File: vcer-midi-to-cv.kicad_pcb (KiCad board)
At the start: 4 copper layers, 140 x 128.5 mm, 109 parts, among them J1 Conn_01x10_Male, J10 CV3, J11 CV4, J12 Vel1, J13 Vel2, J14 Vel3, J15 Vel4, J16 Gate1, J17 Gate2, J18 Gate3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

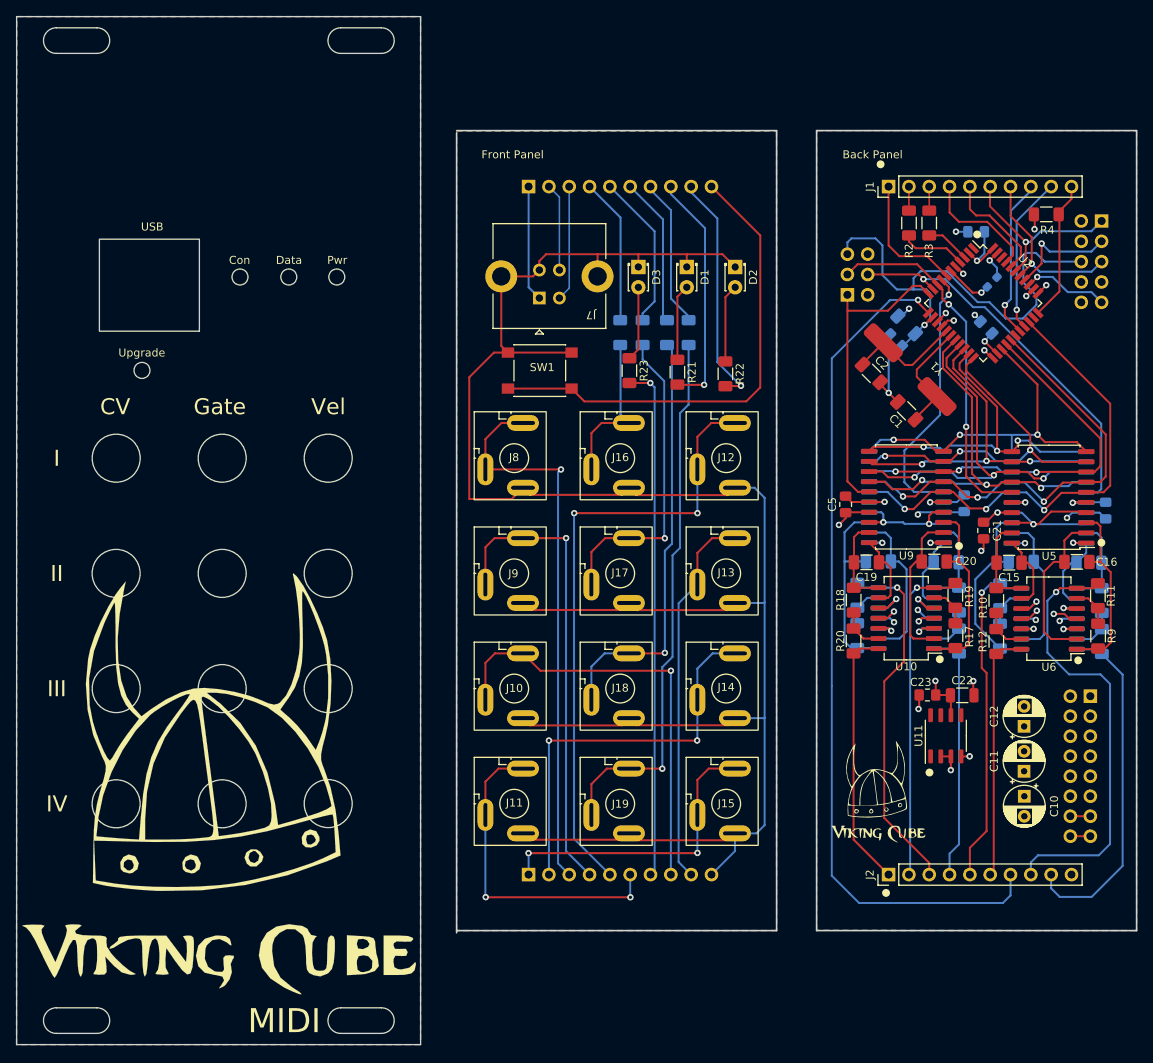
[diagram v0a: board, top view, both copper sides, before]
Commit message: removed other panels
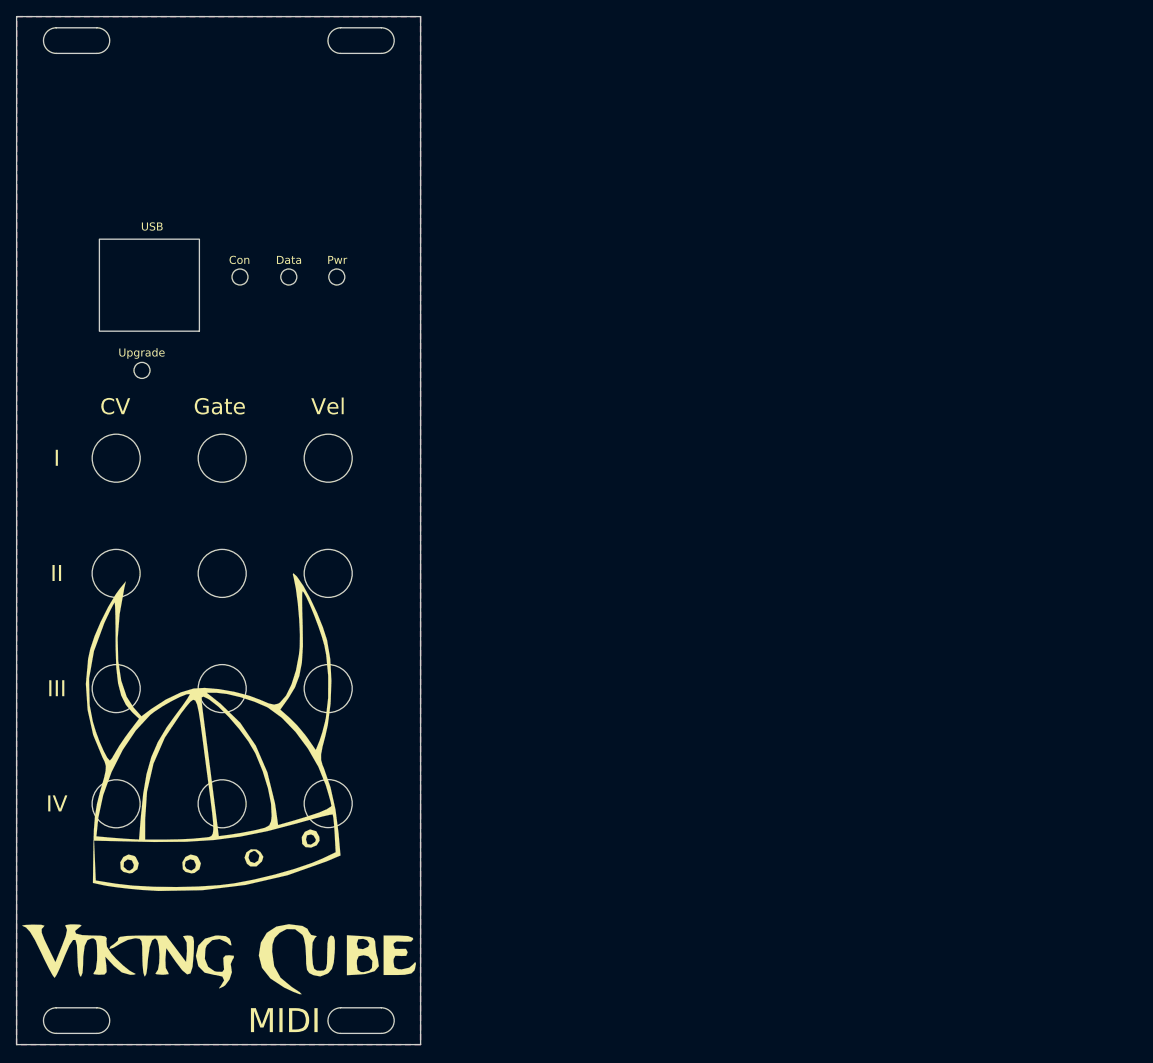
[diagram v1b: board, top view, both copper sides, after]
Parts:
- removed C1, C2: 18pF, Capacitor_SMD:C_1206_3216Metric_Pad1.33x1.80mm_HandSolder
- removed C10, C11, C12: 100uF, Capacitor_THT:CP_Radial_D5.0mm_P2.50mm
- removed C13, C14, C15, C16, C17, C18, C19, C20: 15pF, Capacitor_SMD:C_1206_3216Metric_Pad1.33x1.80mm_HandSolder
- removed C21, C3, C5, C6, C7, C8, C9: 100nF, Capacitor_SMD:C_0805_2012Metric_Pad1.18x1.45mm_HandSolder
- removed C22: 1uF (TANT), Capacitor_SMD:C_1206_3216Metric
- removed C23: 100nF (Ceramic), Capacitor_SMD:C_0805_2012Metric_Pad1.18x1.45mm_HandSolder
- removed C4: 1u, Capacitor_SMD:C_0603_1608Metric_Pad1.08x0.95mm_HandSolder
- removed D1, D2, D3: LED, LED_THT:LED_D1.8mm_W3.3mm_H2.4mm
- removed the G*** at (55.0, 84.6)
- removed the G*** at (6.69, 30.3)
- removed J1, J2: Conn_01x10_Male, Connector_PinHeader_2.54mm:PinHeader_1x10_P2.54mm_Vertical
- removed J10: CV3, eurorack:LUM 1502-03
- removed J11: CV4, eurorack:LUM 1502-03
- removed J12: Vel1, eurorack:LUM 1502-03
- removed J13: Vel2, eurorack:LUM 1502-03
- removed J14: Vel3, eurorack:LUM 1502-03
- removed J15: Vel4, eurorack:LUM 1502-03
- removed J16: Gate1, eurorack:LUM 1502-03
- removed J17: Gate2, eurorack:LUM 1502-03
- removed J18: Gate3, eurorack:LUM 1502-03
- removed J19: Gate4, eurorack:LUM 1502-03
- removed J5: AVR-ISP-6, Connector_PinHeader_2.54mm:PinHeader_2x03_P2.54mm_Vertical
- removed J6: AVR-JTAG-10, Connector_PinHeader_2.54mm:PinHeader_2x05_P2.54mm_Vertical
- removed J7: USB_B, eurorack:USB-BG
- removed J8: CV1, eurorack:LUM 1502-03
- removed J9: CV2, eurorack:LUM 1502-03
- removed R1, R4: 10k, Resistor_SMD:R_1206_3216Metric_Pad1.30x1.75mm_HandSolder
- removed R10, R11, R12, R13, R14, R15, R16, R17, R18, R19, R20, R5, R6, R7, R8, R9: R-10k-1206, Resistor_SMD:R_1206_3216Metric_Pad1.30x1.75mm_HandSolder
- removed R2, R3: 22, Resistor_SMD:R_1206_3216Metric_Pad1.30x1.75mm_HandSolder
- removed R21, R22, R23: R, Resistor_SMD:R_1206_3216Metric_Pad1.30x1.75mm_HandSolder
- removed SW1: Program, Button_Switch_SMD:SW_Push_1P1T_NO_6x6mm_H9.5mm
- removed U1: power_conn_16, eurorack:power_16
- removed U10, U4, U6, U8: TL074, Package_SO:SO-14_5.3x10.2mm_P1.27mm
- removed U11: REF195, Package_SO:SO-8_3.9x4.9mm_P1.27mm
- removed U2: ATmega32U4-A, Package_QFP:TQFP-44_10x10mm_P0.8mm
- removed U3, U5, U7, U9: TLC7528, Package_SO:SOIC-20W_7.5x12.8mm_P1.27mm
- removed Y1: 16Mhz, eurorack:HC49-4HSMX
- removed locked (x4): 470, Resistor_SMD:R_1206_3216Metric_Pad1.30x1.75mm_HandSolder
- removed locked (x2): Conn_01x10_Female, Connector_PinSocket_2.54mm:PinSocket_1x10_P2.54mm_Vertical
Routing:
- net GND: track 393.7 -> 0.00 mm, vias 28 -> 0
- net +5V: track 296.0 -> 0.00 mm, vias 10 -> 0
- net GND2: track 259.1 -> 0.00 mm
- net /L3: track 107.4 -> 0.00 mm, vias 1 -> 0
- net +5F: track 82.8 -> 0.00 mm, vias 4 -> 0
- net +12V: track 77.9 -> 0.00 mm, vias 5 -> 0
- net /fV1: track 77.4 -> 0.00 mm, vias 2 -> 0
- net /fCV1: track 70.1 -> 0.00 mm, vias 1 -> 0
- net Net-(J19-PadT): track 67.9 -> 0.00 mm, vias 1 -> 0
- net /fL3: track 64.5 -> 0.00 mm, vias 1 -> 0
- net -12V: track 64.3 -> 0.00 mm, vias 4 -> 0
- net /reset: track 61.7 -> 0.00 mm, vias 1 -> 0
- net /fPRG: track 60.5 -> 0.00 mm
- net /DACA/B: track 60.5 -> 0.00 mm, vias 3 -> 0
- net /fCV2: track 58.5 -> 0.00 mm, vias 1 -> 0
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- removed copper zone on B.Cu, net GND
- removed copper zone on F.Cu, net GND
- removed copper zone on In1.Cu, net GND
- removed copper zone on B.Cu, net GND2
- removed copper zone on F.Cu, net GND2
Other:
- board size 140 x 128.5 mm -> 50.5 x 128.5 mm
- board text removed: "+12V"
- board text removed: "+45;0"
- board text removed: "+5V"
- board text removed: "-12V"
- board text removed: "Back Panel"
- board text removed: "Front Panel"
- board text removed: "GND"
- board text removed: "ISP"
- board text removed: "JTAG"
- board text removed: "NC"
- board text removed: "RED"
